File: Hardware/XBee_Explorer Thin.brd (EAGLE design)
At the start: 43.2 x 52.1 mm, 129 parts, among them J4 QWIIC_RIGHT_ANGLE, Q2 3.1A/30V/105mΩ, U1 FSUSB30MUX_MSOP10, U2 AP63203, U3 ESD Diode, U5 ESD Diode, U6 CP210X

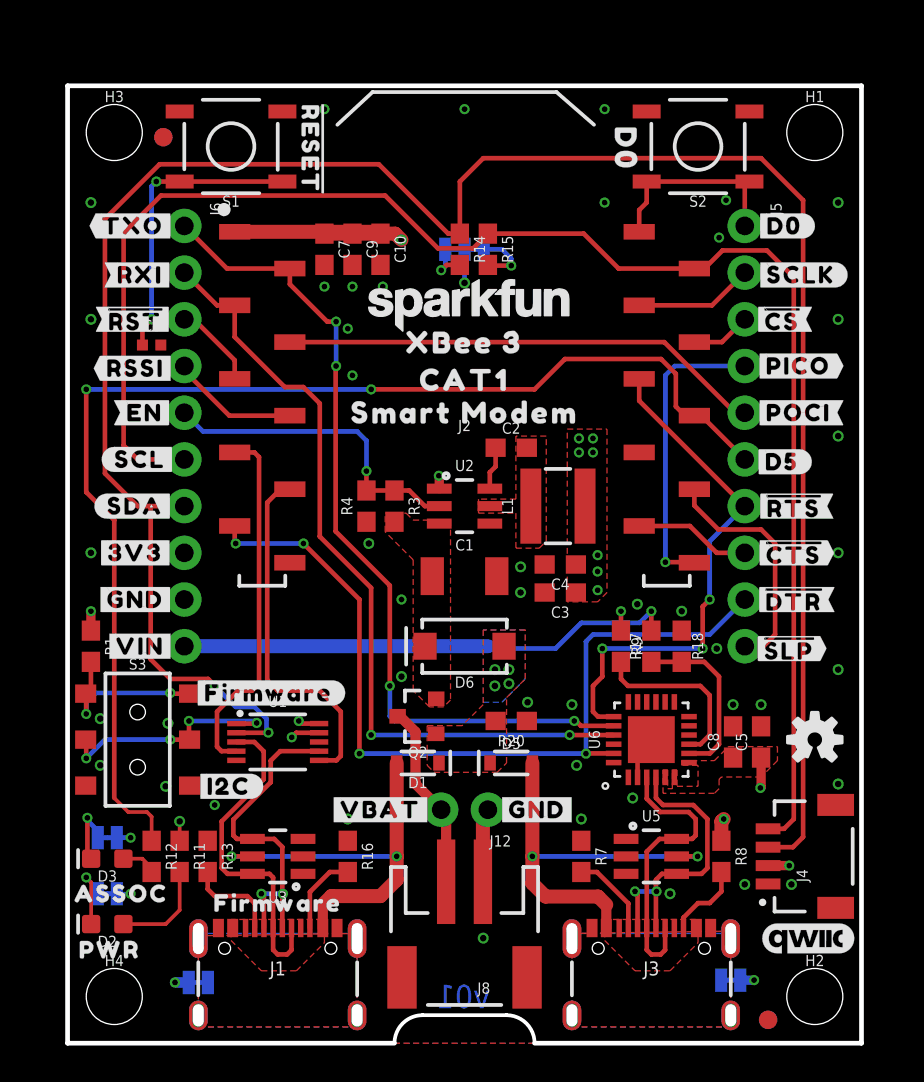
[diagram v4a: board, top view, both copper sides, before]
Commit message: Adds more direct feeback trace for feedback pin on regulator
* Restricts ground pour underneath the inductor (which still needs to be changed)
* Updates USB lines to get closer to a 90 ohm impedance (8 mil, 6mil spacing)
* Removes voltage divider on EN pin that was changing the UVLO threshold.
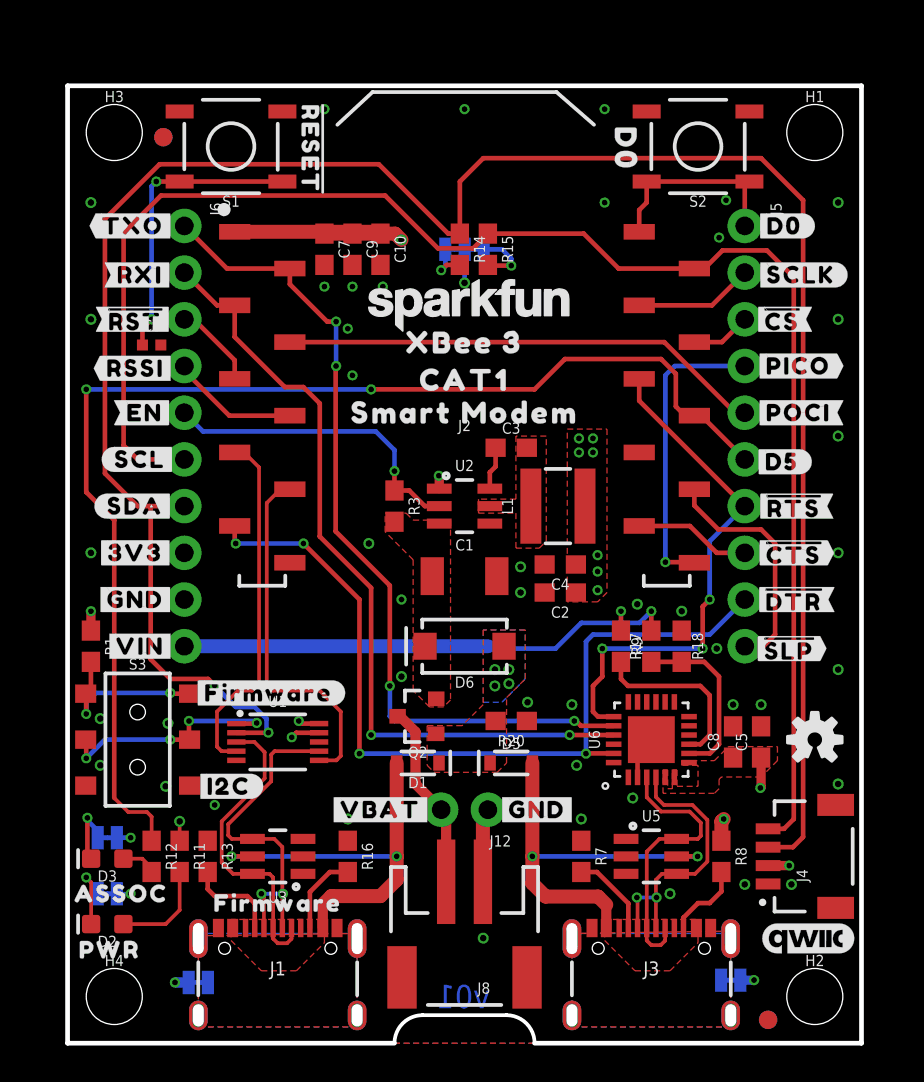
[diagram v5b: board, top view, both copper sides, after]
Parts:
- removed R4: 100k, SparkFun-Resistors:0603
- C2: value 0.1uF -> 22uF
- C3: value 22uF -> 0.1uF
- moved C2 8.31 mm to (26.8, 24.5), turned to 180 degrees
- moved C3 8.31 mm to (24.1, 32.4), turned to 0 degrees
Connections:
- net 3.3V: now also C2.1; no longer C3.1
- net EN: no longer R4.2
- net GND: now also C2.2; no longer C3.2, R4.1
- net N$1: now also C3.1; no longer C2.1
- net N$8: now also C3.2; no longer C2.2
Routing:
- net 3.3V: track 22.0 -> 31.0 mm
- net DIRECT_D+: track 18.3 -> 17.0 mm
- net D-: track 16.0 -> 15.3 mm
- net D+: track 15.9 -> 15.3 mm
- net DIRECT_D-: track 18.2 -> 18.8 mm

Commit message: Updates measures
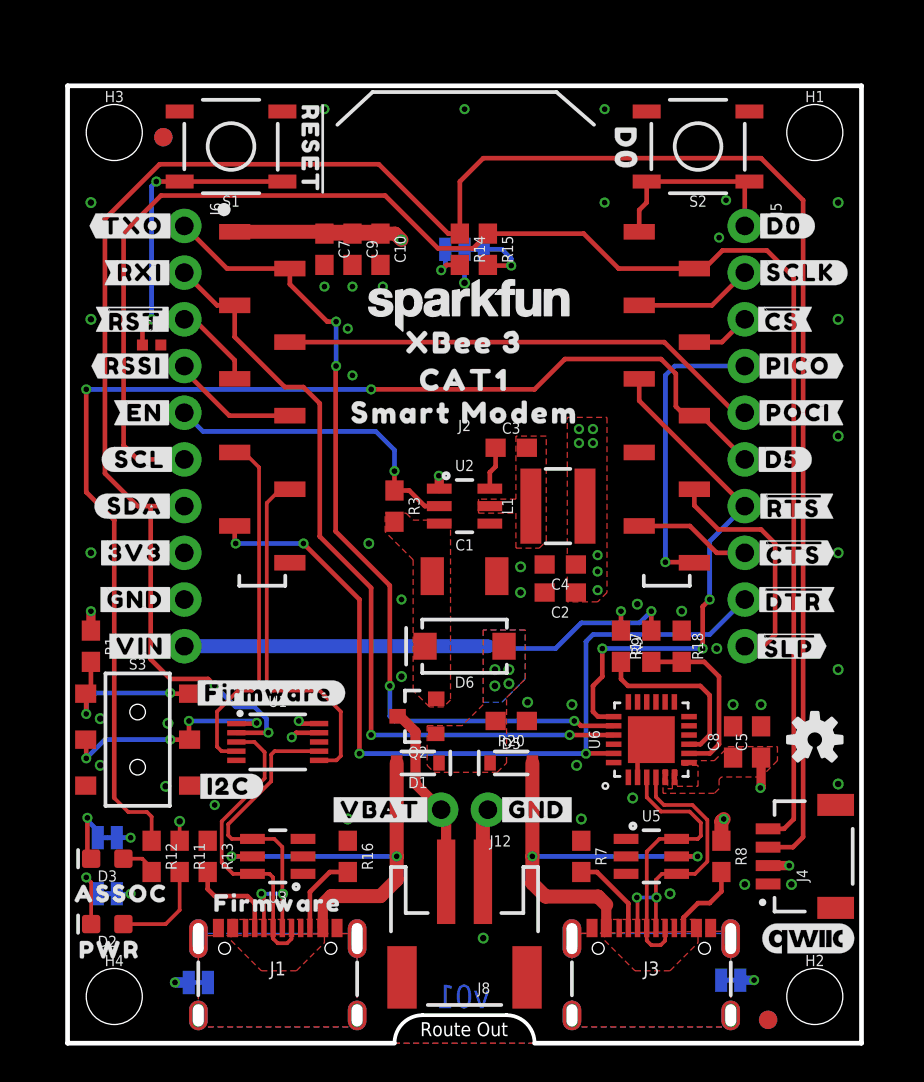
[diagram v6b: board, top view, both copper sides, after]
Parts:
- moved U$60 0.18 mm to (33.0, 21.6)
- moved U$36 0.18 mm to (10.9, 3.30)
- moved U$31 0.18 mm to (3.56, 36.8)
- moved U$21 0.13 mm to (8.51, 34.3)
- moved U$39 0.13 mm to (38.9, 31.8)
- moved U$46 0.13 mm to (8.76, 21.6)
- moved U$47 0.13 mm to (39.2, 21.6)
- moved U$56 0.13 mm to (31.9, 31.8)
- moved U$1 0.13 mm to (3.94, 41.9)
- moved U$12 0.13 mm to (32.6, 39.4)
- moved U$16 0.13 mm to (10.5, 41.9)
- moved U$18 0.13 mm to (10.8, 36.8)
- moved U$33 0.13 mm to (39.9, 41.9)
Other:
- board text added: "Route Out"

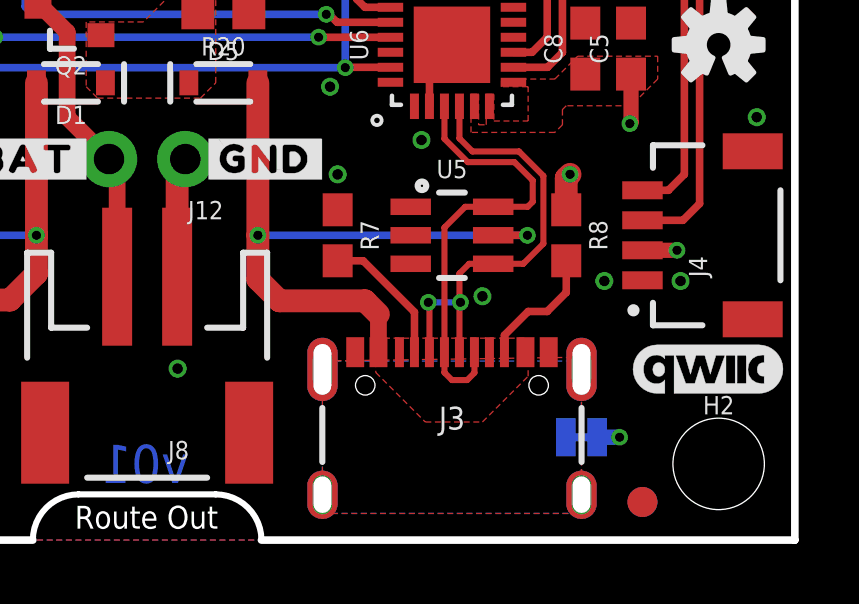
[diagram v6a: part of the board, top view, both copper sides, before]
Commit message: Adds "UART" silk for other USB connector
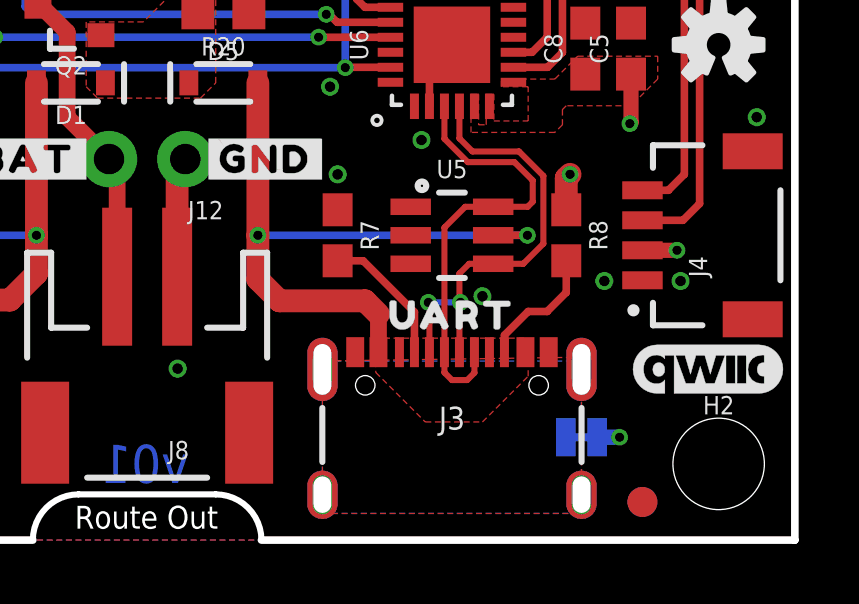
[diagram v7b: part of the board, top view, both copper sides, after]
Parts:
- added U$65: (no value), top:UART32
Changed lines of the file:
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@@
 <layer number="39" name="tKeepout" color="4" fill="11" visible="no" active="yes"/>
 <layer number="40" name="bKeepout" color="1" fill="11" visible="no" active="yes"/>
-<layer number="41" name="tRestrict" color="4" fill="10" visible="no" active="yes"/>
-<layer number="42" name="bRestrict" color="1" fill="10" visible="no" active="yes"/>
-<layer number="43" name="vRestrict" color="2" fill="10" visible="no" active="yes"/>
+<layer number="41" name="tRestrict" color="4" fill="10" visible="yes" active="yes"/>
+<layer number="42" name="bRestrict" color="1" fill="10" visible="yes" active="yes"/>
+<layer number="43" name="vRestrict" color="2" fill="10" visible="yes" active="yes"/>
 <layer number="44" name="Drills" color="7" fill="1" visible="no" active="yes"/>
 <layer number="45" name="Holes" color="7" fill="1" visible="yes" active="yes"/>
-<layer number="46" name="Milling" color="3" fill="1" visible="yes" active="yes"/>
+<layer number="46" name="Milling" color="3" fill="1" visible="no" active="yes"/>
 <layer number="47" name="Measures" color="7" fill="1" visible="yes" active="yes"/>
 <layer number="48" name="Document" color="7" fill="1" visible="no" active="yes"/>
@@
 <element name="U$64" library="top" package="MODEM1338" value="" x="21.59" y="29.21" smashed="yes" rot="MR0"/>
 <element name="U$48" library="bot" package="#FIRMWARE#31" value="" x="10.922" y="19.05" smashed="yes"/>
+<element name="U$65" library="top" package="UART32" value="" x="31.75" y="7.493" smashed="yes"/>
 </elements>
 <signals>

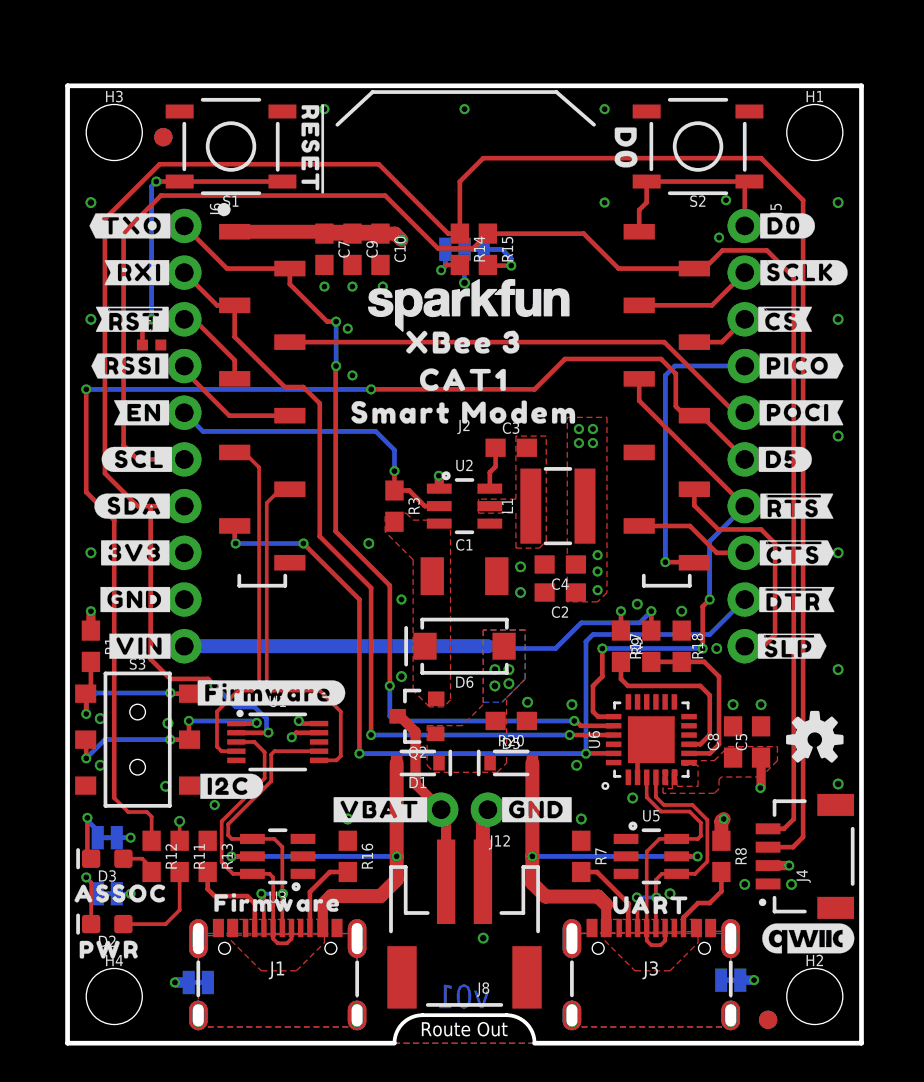
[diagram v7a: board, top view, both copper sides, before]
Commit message: Updates footprint to include module outline, increases size of board, moves buttons
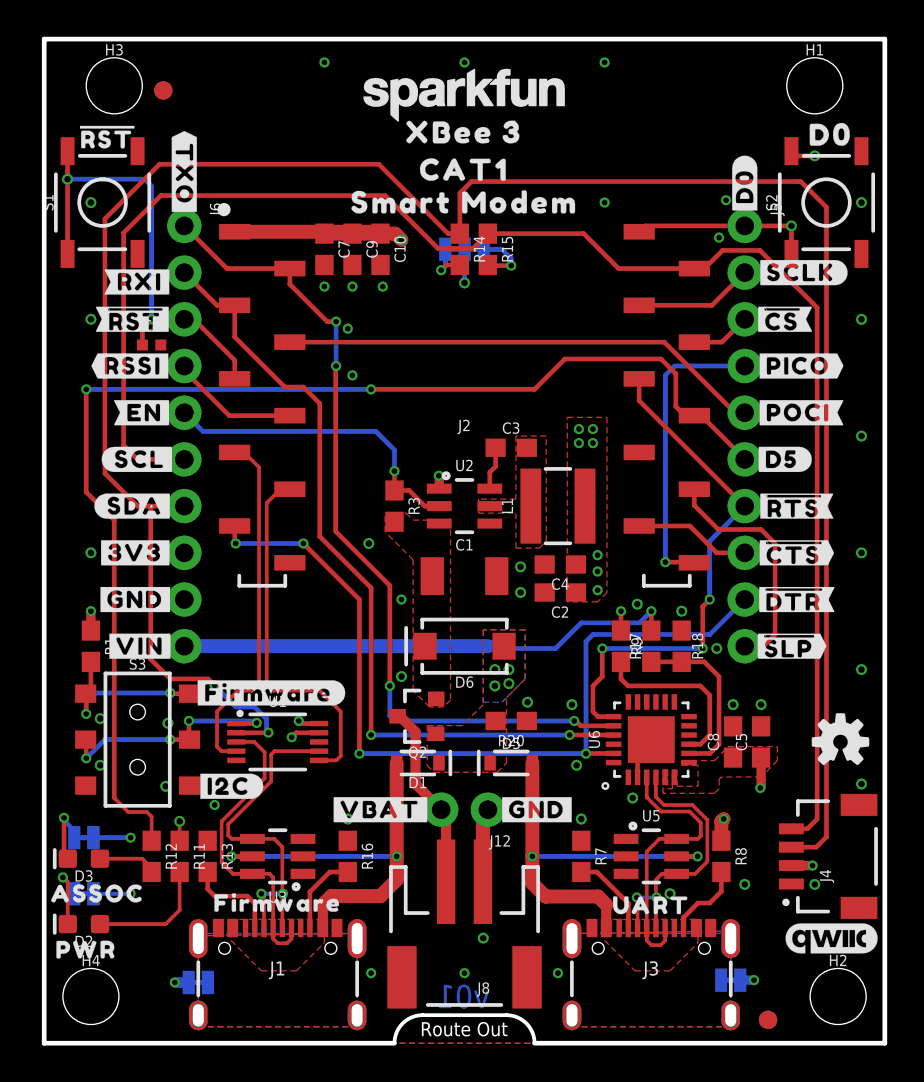
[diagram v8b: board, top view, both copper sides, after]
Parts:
- U$30: device top:#RESET#28 -> top:#RST#30
- U$63: device SparkFun-Aesthetics:SFE_LOGO_NAME_.1 -> SparkFun-Aesthetics:SFE_LOGO_NAME_.2
- moved LOGO1 11.4 mm to (21.6, 51.6)
- moved U$23 11.4 mm to (21.6, 49.5)
- moved U$51 11.4 mm to (21.6, 45.7)
- moved U$52 11.4 mm to (21.6, 47.5)
- moved U$40 11.2 mm to (41.5, 49.4), turned to 0 degrees
- moved U$30 11.2 mm to (2.16, 49.3), turned to 0 degrees
- moved U$63 10.2 mm to (21.6, 49.5)
- moved S1 7.62 mm to (1.91, 45.7), turned to 90 degrees
- moved S2 7.62 mm to (41.3, 45.7), turned to 90 degrees
- moved U$50 3.95 mm to (6.35, 47.2), turned to 270 degrees
- moved U$64 3.81 mm to (21.6, 33.0)
- moved U$53 3.81 mm to (21.6, 39.4)
- moved U$61 3.81 mm to (21.6, 36.8)
- moved U$62 3.81 mm to (21.6, 34.5)
- moved U$10 3.05 mm to (36.8, 46.6), turned to 90 degrees
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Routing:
- net D0: track 11.0 -> 15.6 mm, vias 0 -> 2
- net !RESET!: track 22.5 -> 25.6 mm
- net GND: track 12.2 -> 14.8 mm, vias 51 -> 54
- net N$7: track 5.45 -> 6.72 mm
- net N$12: track 1.96 -> 3.23 mm
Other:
- board size 43.2 x 52.1 mm -> 45.7 x 54.6 mm
